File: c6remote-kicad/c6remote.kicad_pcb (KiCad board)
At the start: 2 copper layers, 37 x 130 mm, 50 parts, among them J1 Battery, Q1 MMBT2222A, Q2 AO3401A, SW1 SW_Push, SW10 SW_Push, SW11 SW_Push, SW2 SW_Push, SW3 SW_Push, SW4 SW_Push, SW5 SW_Push, SW6 SW_Push, SW7 SW_Push, SW8 SW_Push, SW9 SW_Push, U1 XIAO-ESP32-C6, U2 TSOP4136, U3 PCF8575DBR

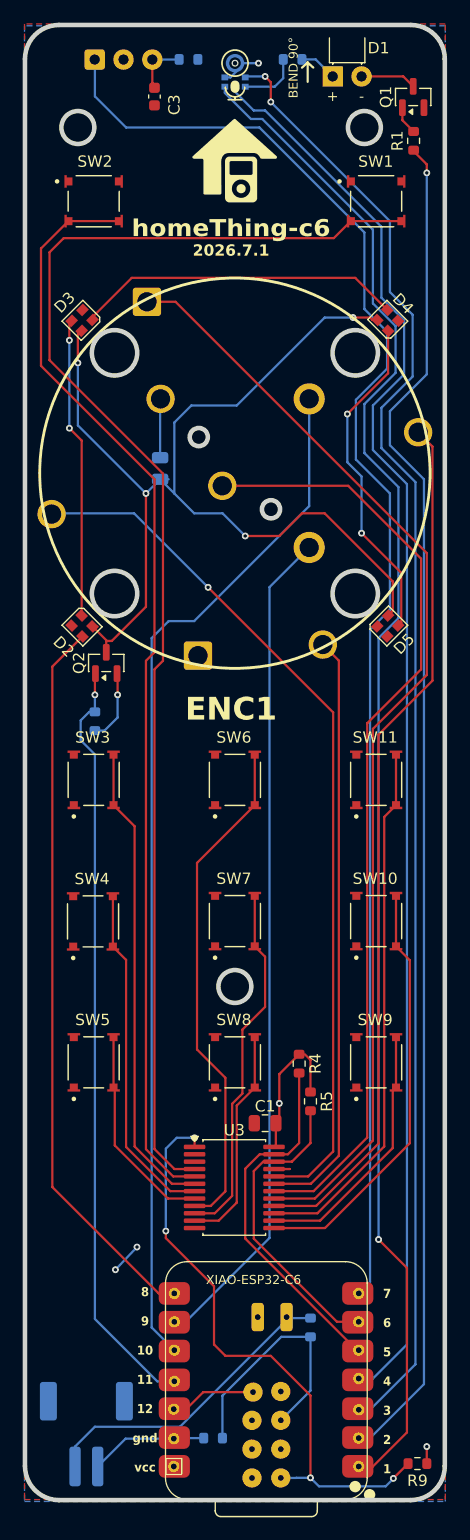
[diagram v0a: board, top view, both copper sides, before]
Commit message: fix(pcb): rework the board for PCBWay's second via-in-pad report, delete all 14 TP_* test points, retire the VCC rail, and bump the front silk to 2026.8.0, taking DRC to 1 warning and schematic parity to 0; PCBWay reported vias in pad against the newer files, which does not reproduce, so scripts/check-via-in-pad.py now sweeps every via centre plus annular ring against every pad rectangle layer-agnostically and confirms the four originals sit dead centre in R9.1, R9.2, SW11.2 and U3.1 at -0.300mm on 1693423^ while 2026.7.1 and this board have zero overlaps, closest approach 0.305mm at U3 pin 1, so their marked-up file is what is needed to close it out; board side, vias moved clear, tracks tidied, vias 24 to 33 and segments 343 to 355, R8 moved from 51.415,152.75 rot 180 to 52.75,153.25 rot -90, the 14 TP_* footprints deleted, which also clears the silk_overlap warning and the 13 extra_footprint parity issues, and VCC is retired because it had shrunk to the U1/14 VBUS node alone, so the schematic pin now carries a no-connect and the board reads unconnected-(U1-VBUS-Pad14); ERC 0, DRC 0 errors and 0 unconnected with only the U1 lib_footprint_mismatch left, parity 0, zones reproduce their stored fill to 0.0000mm2 so the GUI refill is saved, position file still 35 rows with 0 test points and BOM output byte-identical to 2026.7.1, the answer PCBWay asked for; docs follow the new baseline, and AGENTS.md now says power splits two ways with no probe pad on any signal
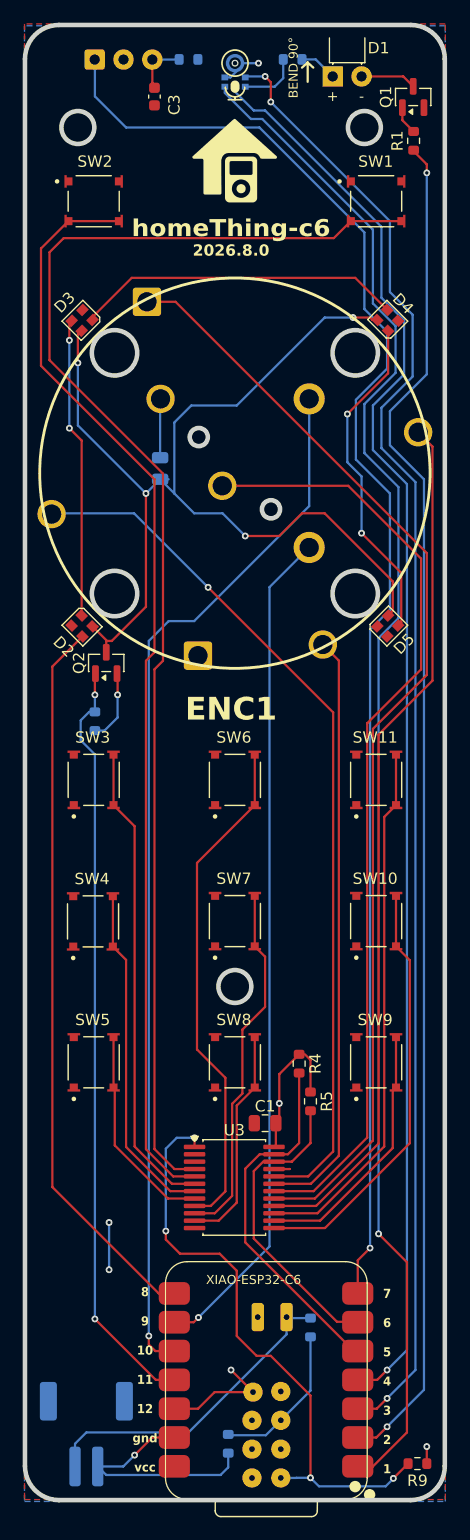
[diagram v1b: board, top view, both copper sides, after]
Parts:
- removed TP_3V3, TP_ANO_ENC1, TP_ANO_ENC2, TP_GND, TP_GPIO18_D10_MOSI, TP_IR_EMIT, TP_IR_REC, TP_LED1, TP_SCK, TP_SCL, TP_SD, TP_SDA, TP_VCC1, TP_WS: TestPoint_THTPad_1.0x1.0mm_Drill0.5mm_NoCrtYd, Local:TestPoint_THTPad_1.0x1.0mm_Drill0.5mm_NoCrtYd
- moved R8 1.43 mm to (52.8, 153.2), turned to -90 degrees
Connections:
- U1 pad 14: VCC -> unconnected-(U1-VBUS-Pad14)
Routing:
- net GND: track 23.3 -> 35.5 mm, vias 3 -> 4
- net bat_sense: track 22.1 -> 13.7 mm
- net +3.3V: track 33.4 -> 36.1 mm, vias 3 -> 4
- net ano_enc1: track 91.8 -> 93.0 mm, vias 0 -> 1
- net BAT: track 27.4 -> 28.3 mm
- net sd: track 125.5 -> 125.9 mm, vias 0 -> 1
- net ano_enc2: track 73.8 -> 74.2 mm, vias 0 -> 1
- net IR EMIT: track 119.6 -> 120.0 mm, vias 1 -> 2
- net sck: track 129.8 -> 130.2 mm, vias 2 -> 3
- net led_en: track 67.5 -> 67.4 mm, vias 1 -> 2
- net IR REC: track 129.8 -> 129.9 mm, vias 0 -> 1
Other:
- board text added: "2026.8.0"
- board text removed: "2026.7.1"

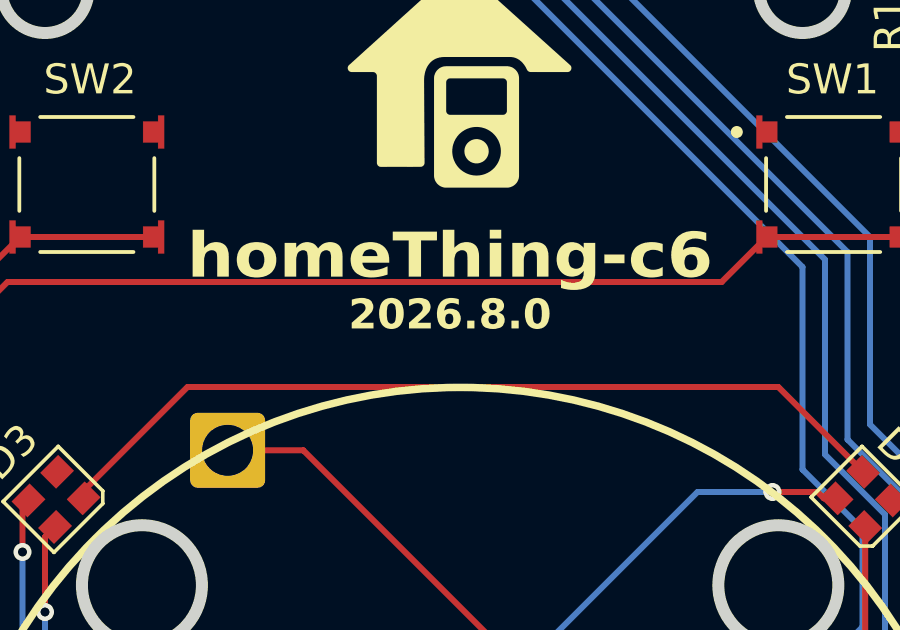
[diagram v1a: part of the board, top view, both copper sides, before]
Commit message: fix(pcb): reword back silk origin line to designed in Vancouver Canada and bump front silk revision to 2026.8.1, since 2026.8.0 is already released so this artwork would otherwise ship under a version the silk does not show; silkscreen only with no copper touched, the line stays bottom-justified at y 105.5 on the board axis so the stack above the flag and the flag clearance are unchanged, and the now-wider second line measures 20.286mm against 20.219mm for homething.io above it, leaving 8.2mm to the left board edge and 8.5mm to the right; ERC 0, DRC 1 warning (lib_footprint_mismatch on U1) and parity 0, no zone refill needed
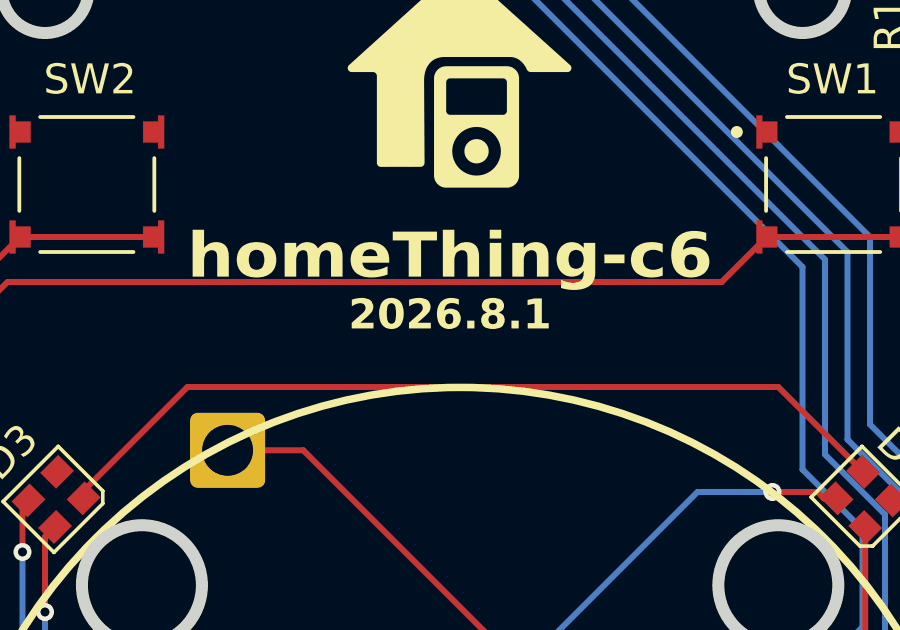
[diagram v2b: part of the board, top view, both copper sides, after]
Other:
- board text added: "2026.8.1"
- board text added: "designed in Vancouver Canada"
- board text removed: "2026.8.0"
- board text removed: "made in Vancouver Canada"
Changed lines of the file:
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@@
 		)
 	)
-	(gr_text "2026.8.0"
+	(gr_text "2026.8.1"
 		(at 53 47.5 0)
 		(layer "F.SilkS")
@@
 			(justify top)
 		)
-		(render_cache "2026.8.0" 0
+		(render_cache "2026.8.1" 0
 			(polygon
 				(pts
@@
 			(polygon
 				(pts
-					(xy 55.736928 47.468672) (xy 55.797388 47.480529) (xy 55.847506 47.498909) (xy 55.893501 47.525631)
-					(xy 55.933518 47.559706) (xy 55.968101 47.601735) (xy 55.99537 47.648134) (xy 56.017932 47.702837)
-					(xy 56.035389 47.767088) (xy 56.050671 47.869245) (xy 56.056211 47.993257) (xy 56.050539 48.120911)
-					(xy 56.035023 48.224188) (xy 56.017311 48.288897) (xy 55.994638 48.343567) (xy 55.967429 48.389541)
-					(xy 55.933308 48.430133) (xy 55.893206 48.463335) (xy 55.846468 48.489619) (xy 55.795732 48.507716)
-					(xy 55.735528 48.519308) (xy 55.66414 48.523447) (xy 55.593173 48.519317) (xy 55.533135 48.507734)
-					(xy 55.482363 48.489619) (xy 55.435721 48.463273) (xy 55.395399 48.429631) (xy 55.360791 48.388136)
-					(xy 55.333512 48.341793) (xy 55.310852 48.287206) (xy 55.293197 48.22315) (xy 55.277688 48.120865)
-					(xy 55.272038 47.9946) (xy 55.528158 47.9946) (xy 55.532687 48.120301) (xy 55.544083 48.204635)
-					(xy 55.559543 48.25826) (xy 55.578976 48.293723) (xy 55.602434 48.317211) (xy 55.630324 48.331065)
-					(xy 55.66414 48.335868) (xy 55.697923 48.331066) (xy 55.725783 48.317215) (xy 55.749212 48.293728)
-					(xy 55.768615 48.25826) (xy 55.784089 48.204605) (xy 55.795515 48.119892) (xy 55.800061 47.993257)
-					(xy 55.795538 47.865619) (xy 55.784218 47.781083) (xy 55.768982 47.728253) (xy 55.749789 47.693556)
-					(xy 55.726401 47.670457) (xy 55.698364 47.656758) (xy 55.66414 47.651988) (xy 55.630232 47.656736)
-					(xy 55.602319 47.670404) (xy 55.578902 47.693502) (xy 55.559543 47.728253) (xy 55.544171 47.781123)
-					(xy 55.532734 47.866034) (xy 55.528158 47.9946) (xy 55.272038 47.9946) (xy 55.272008 47.993928)
-					(xy 55.27767 47.863606) (xy 55.29283 47.762997) (xy 55.310318 47.700661) (xy 55.333523 47.646077)
-					(xy 55.362195 47.598316) (xy 55.39726 47.556896) (xy 55.438025 47.523502) (xy 55.48511 47.497566)
-					(xy 55.536261 47.479713) (xy 55.595484 47.468406) (xy 55.66414 47.46441)
+					(xy 56.024093 48.5) (xy 55.351937 48.5) (xy 55.351937 48.324145) (xy 55.566382 48.324145) (xy 55.566382 47.784856)
+					(xy 55.351937 47.784856) (xy 55.351937 47.620725) (xy 55.445482 47.61468) (xy 55.489354 47.606205)
+					(xy 55.519976 47.595141) (xy 55.549384 47.575886) (xy 55.570779 47.551666) (xy 55.584784 47.521996)
+					(xy 55.591661 47.483949) (xy 55.814411 47.483949) (xy 55.814411 48.324145) (xy 56.024093 48.324145)
 				)
 			)
@@
 		)
 	)
-	(gr_text "made in Vancouver\nCanada"
+	(gr_text "designed in\nVancouver Canada"
 		(at 53.337455 105.5 0)
 		(layer "B.SilkS")

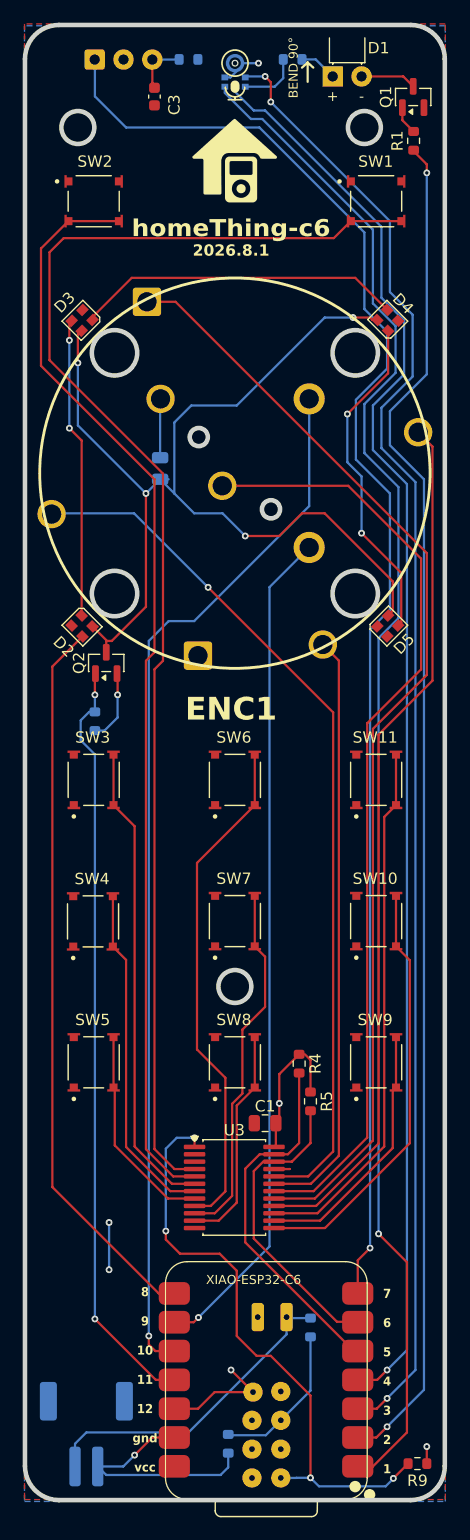
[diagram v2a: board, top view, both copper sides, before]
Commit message: feat(pcb): gate the IR receiver rail behind Q3 and R11 on a new ir_vdd net with ir_en on GPIO6, taking the deep-sleep floor from ~0.41mA to ~58uA and standby on a 1000mAh cell from 82 days to 575, because U2 was 88% of the standby draw at 350uA continuous while listening for something that cannot wake the board, IR REC sitting on GPIO16 outside the C6's GPIO0-GPIO7 wake range; Q3 is a second AO3401A with source on +3.3V and drain on ir_vdd, R11 a 1M gate pull-up holding the rail off by default, and R6's upper end moves off +3.3V so the gate sits upstream of the existing R6/C3 filter, which stays with U2 untouched and is why no reservoir cap is needed unlike C4 on the LED rail; Q3 and R11 sit beside U1 rather than U2, the opposite of Q2, because ir_en is a 1M high-impedance node whenever GPIO6 is an input so the whole net is kept short while ir_vdd takes the 110mm run at 350uA of DC for 0.2mV of drop; the first routing attempt pinched the F.Cu GND pour into unreachable pieces, the same trap led_vdd hit, fixed with stitching vias so the pour is now 3 mutually reachable regions of 1882.9, 695.6 and 375.8mm2 against a single 3220.8mm2 B.Cu +3.3V plane; firmware gains an IR Rail switch on GPIO6, inverted like led_rail but ALWAYS_ON rather than ALWAYS_OFF since remote_receiver cannot decode with U2 unpowered and switching it off while awake only leaks ~44uA back through GPIO16's pullup into U2's internal 30k, so the saving is real only in deep sleep where the pullup is released; ERC 0, DRC 1 warning (the inherited U1 lib_footprint_mismatch), 0 unconnected and parity 0, all four ESPHome configs valid, position file 37 rows and the BOM groups Q3 with Q2 and R11 with R10; silk stays 2026.8.1, which is exactly what the next push to main computes; docs add the board's first power budget with datasheet currents for every always-on part, and AGENTS.md now bans the MCP sync_schematic_to_board outright after it corrupted 16 existing pad nets, including rotating MK1 1/2/4/6 back in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
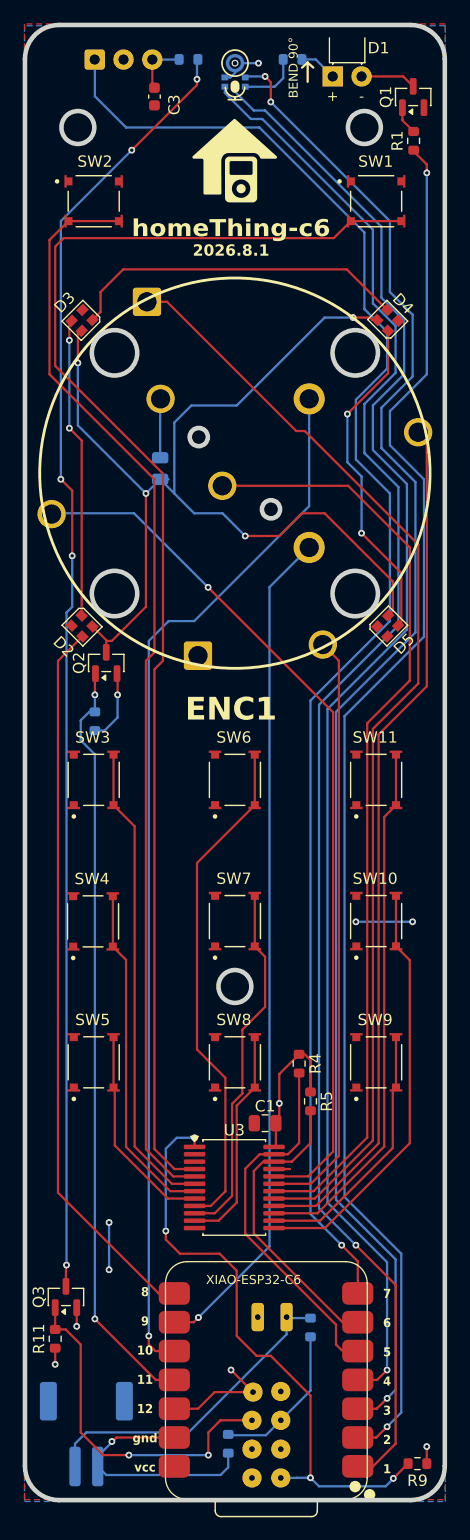
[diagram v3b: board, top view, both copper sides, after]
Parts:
- added Q3: AO3401A, Package_TO_SOT_SMD:SOT-23, F.Cu at (38.5, 140.3)
- added R11: 1M, Resistor_SMD:R_0603_1608Metric, F.Cu at (37.5, 144.0)
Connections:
- R6 pad 1: +3.3V -> ir_vdd
- U1 pad 29: unconnected-(U1-GPIO6_MTCK-Pad29) -> ir_en
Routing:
- net ir_vdd: track 0.00 -> 113.8 mm, vias 0 -> 5
- net ir_en: track 0.00 -> 30.8 mm, vias 0 -> 2
- net GND: track 35.5 -> 41.0 mm, vias 4 -> 6
- net sd: track 125.9 -> 130.3 mm
- net sck: track 130.2 -> 134.5 mm
- net IR EMIT: track 120.0 -> 124.1 mm
- net ws: track 135.1 -> 138.7 mm
- net IR REC: track 129.9 -> 133.3 mm
- net +3.3V: track 36.1 -> 39.2 mm, vias 4 -> 6
- net led_3: track 28.8 -> 30.3 mm
- net ano_sw3: track 83.3 -> 82.5 mm
- net sw2: track 97.0 -> 96.4 mm
- net ano_sw2: track 98.4 -> 97.8 mm
- net sda: track 32.4 -> 33.0 mm

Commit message: feat(pcb): move the bottom M2.5 mounting hole off the centreline at 53.337,112.95 down to 38.25,132 and add a second at 68.5,132, so a case screws into four points instead of three and the bottom pair straddles the board 30.25mm apart at 3.4mm and 3.3mm from the side edges rather than one screw pulling on the centreline 45mm above the bottom edge; both are 2.9mm Edge.Cuts circles matching the top pair for loose M2.5 metal screws, and the copper moved rather than the holes taking clearance from it, 29 segments out and 33 in across led_vdd, led_1, led_en, ir_vdd, sw1, sw2 and GND for +3.7mm of track overall, with the two GND stitching vias at 42.25,133.75 and 42.25,137.914 relocated to 38.75,124 and 38.75,127, led_en's via from 41,142.25 to 43,144.25 and led_vdd's from 39.5,58 to 39.5,58.5; zones were refilled in the GUI and reproduce under --refill-zones, DRC 1 warning (the inherited U1 lib_footprint_mismatch), 0 unconnected and parity 0, and the silk stays 2026.8.1 which is still what the next push to main computes since 2026.8.0 is the newest tag
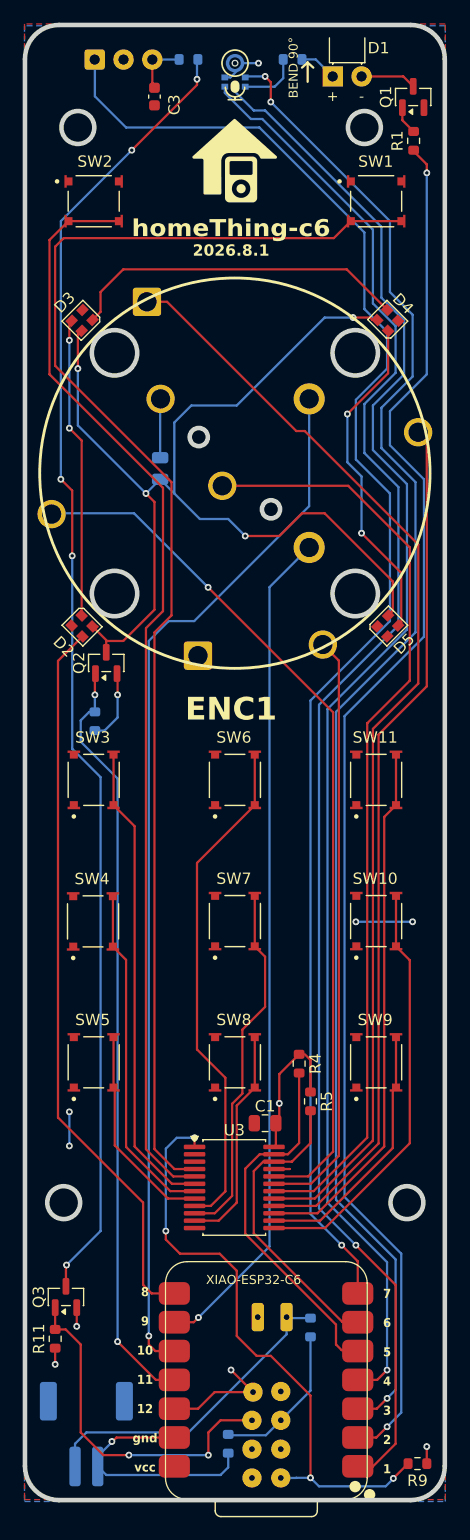
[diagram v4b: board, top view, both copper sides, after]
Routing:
- net ir_vdd: track 113.8 -> 115.8 mm
- net led_vdd: track 94.5 -> 95.8 mm
- net GND: track 41.0 -> 39.9 mm
- net sw1: track 119.5 -> 120.1 mm
- net sw2: track 96.4 -> 97.0 mm
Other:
- outline, holes or cut-outs redrawn
